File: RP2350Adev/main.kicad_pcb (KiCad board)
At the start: 4 copper layers, 88.9 x 50.9 mm, 111 parts, among them J1 J-Link, J2 SPI Pins, J3 QSPI Pins, J4 UART Pins, J5 UART, J6 DEBUG, J7 USB_A_Male, J8 USB_A_Female, J9 USB4105-GF-A, M1 TS3USB3031RMGR, SW1 SW_DIP_x06, U1 nRF5340-QKxx, U3 LFD_Diplexer, U4 nRF7002-QFAA, U6 W25Q32JV, U7 RP2350A, U8 TS3USB30EDGSR, X1 32.768kHz, X2 32MHz, X3 XTAL-40, X4 IQXO-791

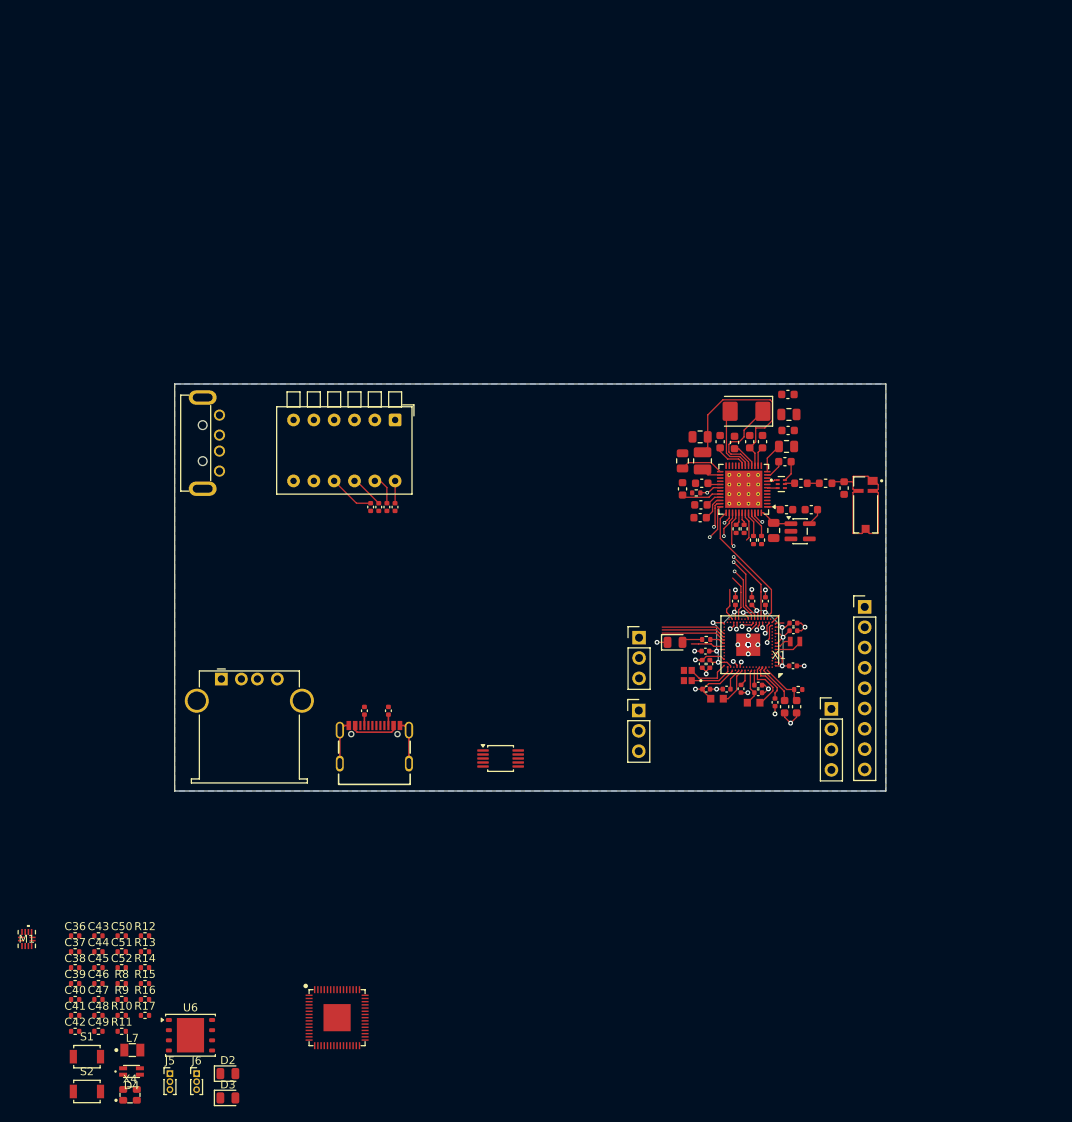
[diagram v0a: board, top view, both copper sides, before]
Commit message: Combine subcircuits
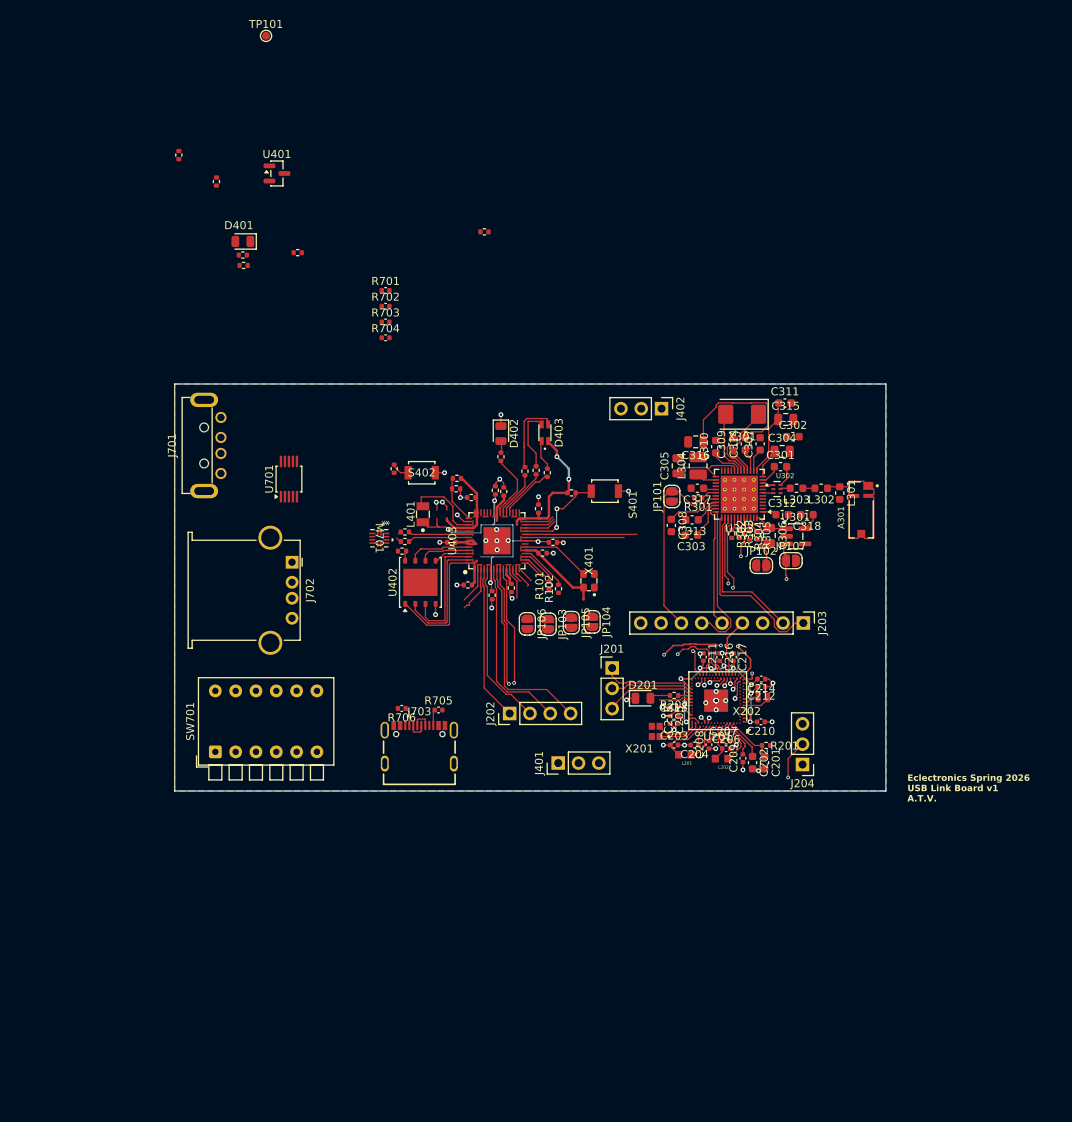
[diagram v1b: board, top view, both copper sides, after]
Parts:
- removed A1: NN03-320, Eclectronics:XCVR_NN03-320
- removed C1, C17, C7, C8, C9: 1.0µF, Capacitor_SMD:C_0402_1005Metric
- removed C10, C9: 100nF, Capacitor_SMD:C_0603_1608Metric
- removed C10, C11, C12, C13, C16, C3, C4, C5, C6: 100nF, Capacitor_SMD:C_0402_1005Metric
- removed C11, C12, C22, C23: 4.7uF, Capacitor_SMD:C_0805_2012Metric
- removed C13: 2.2uF, Capacitor_SMD:C_0805_2012Metric
- removed C14: 22nF, Capacitor_SMD:C_0603_1608Metric
- removed C14, C15: 4.7µF, Capacitor_SMD:C_0603_1608Metric
- removed C15: 0.22uF, Capacitor_SMD:C_0603_1608Metric
- removed C16, C25: 2.2uF, Capacitor_SMD:C_0603_1608Metric
- removed C17, C18, C19, C20: 1uF, Capacitor_SMD:C_0603_1608Metric
- removed C2: 2.2nF, Capacitor_SMD:C_0402_1005Metric
- removed C21, C8: 0.47uF, Capacitor_SMD:C_0603_1608Metric
- removed C24: 10nF, Capacitor_SMD:C_0603_1608Metric
- removed C36, C38: 10µF, Resistor_SMD:R_0402_1005Metric
- removed C37, C41, C42, C43, C44, C45, C46, C47, C50, C52: 0.1µF, Resistor_SMD:R_0402_1005Metric
- removed C39, C40, C48, C49, C51: 4.7µF, Resistor_SMD:R_0402_1005Metric
- removed D1, D3: LED, LED_SMD:LED_0805_2012Metric
- removed D2: PWR, LED_SMD:LED_0805_2012Metric
- removed D4: IN-S85TATRGB, Eclectronics:IN-S85TATRGB
- removed J1: J-Link, Connector_PinHeader_2.54mm:PinHeader_1x03_P2.54mm_Vertical
- removed J2: SPI Pins, Connector_PinHeader_2.54mm:PinHeader_1x04_P2.54mm_Vertical
- removed J3: QSPI Pins, Connector_PinHeader_2.54mm:PinHeader_1x09_P2.54mm_Vertical
- removed J4: UART Pins, Connector_PinHeader_2.54mm:PinHeader_1x03_P2.54mm_Vertical
- removed J5: UART, Connector_PinHeader_1.00mm:PinHeader_1x03_P1.00mm_Vertical
- removed J6: DEBUG, Connector_PinHeader_1.00mm:PinHeader_1x03_P1.00mm_Vertical
- removed J7: USB_A_Male, Eclectronics:USB_A_0480370001
- removed J8: USB_A_Female, Connector_USB:USB_A_Stewart_SS-52100-001_Horizontal
- removed J9: USB4105-GF-A, Eclectronics:USB4105-GF-A
- removed L1: 10uH, Eclectronics:INDC1608X95N
- removed L2: 10µH, Eclectronics:INDC1608X95N
- removed L3: 7.5nH, Inductor_SMD:L_0603_1608Metric
- removed L4, L5: 2.7nH, Inductor_SMD:L_0603_1608Metric
- removed L6: 3.3uH, Inductor_SMD:L_1008_2520Metric
- removed L7: 3.3µH, Eclectronics:AOTA-B201610S3R3-101-T
- removed M1: TS3USB3031RMGR, Eclectronics:RMG12_TEX
- removed R1, R10, R14, R16, R17: 1K, Resistor_SMD:R_0402_1005Metric
- removed R11, R12: 27Ω, Resistor_SMD:R_0402_1005Metric
- removed R13: 33Ω, Resistor_SMD:R_0402_1005Metric
- removed R15, R8, R9: 5.1K, Resistor_SMD:R_0402_1005Metric
- removed R18, R19, R20, R21: 10K, Capacitor_SMD:C_0402_1005Metric
- removed R2: 2.2 Ω, Resistor_SMD:R_0402_1005Metric
- removed R22, R23: 5.1K, Capacitor_SMD:C_0402_1005Metric
- removed R3, R4, R5, R6, R7: 100k, Resistor_SMD:R_0402_1005Metric
- removed S1: RST, Button_Switch_SMD:SW_SPST_B3U-1000P
- removed S2: BOOT, Button_Switch_SMD:SW_SPST_B3U-1000P
- removed SW1: SW_DIP_x06, Button_Switch_THT:SW_DIP_SPSTx06_Piano_10.8x16.8mm_W7.62mm_P2.54mm
- removed U1: nRF5340-QKxx, Package_DFN_QFN:Nordic_AQFN-94-1EP_7x7mm_P0.4mm
- removed U2: ~, Package_TO_SOT_SMD:SC-74A-5_1.55x2.9mm_P0.95mm
- removed U3: LFD_Diplexer, Eclectronics:FIL_LFD182G45DCJD247
- removed U4: nRF7002-QFAA, Package_DFN_QFN:QFN-48-1EP_6x6mm_P0.4mm_EP4.66x4.66mm_ThermalVias
- removed U6: W25Q32JV, Package_SON:WSON-8-1EP_6x5mm_P1.27mm_EP3.4x4.3mm
- removed U7: RP2350A, Eclectronics:RP2350A_QFN-60_EP_7.75x7.75_Pitch0.4mm
- removed U8: TS3USB30EDGSR, Package_SO:VSSOP-10_3x3mm_P0.5mm
- removed X1: 32.768kHz, Eclectronics:XTAL_CM9V-T1A-32.768KHZ-9PF-20PPM-TA-QC
- removed X2: 32MHz, Eclectronics:XTAL_ABM11W-32.0000MHZ-8-D1X-T3
- removed X3: XTAL-40, Crystal:Crystal_SMD_Abracon_ABM3-2Pin_5.0x3.2mm
- removed X4: IQXO-791, Eclectronics:IQXO-791
- added A301: NN03-320, Eclectronics:XCVR_NN03-320, F.Cu at (129.6, 104.0)
- added C201: 4.7µF, Capacitor_SMD:C_0603_1608Metric, F.Cu at (117.5, 135.7)
- added C202: 4.7µF, Capacitor_SMD:C_0603_1608Metric, F.Cu at (116.0, 135.7)
- added C203: 1.0µF, Capacitor_SMD:C_0402_1005Metric, F.Cu at (106.2, 133.4)
- added C204: 100nF, Capacitor_SMD:C_0402_1005Metric, F.Cu at (108.8, 133.4)
- added C205: 2.2nF, Capacitor_SMD:C_0402_1005Metric, F.Cu at (105.8, 130.3)
- added C206: 1.0µF, Capacitor_SMD:C_0402_1005Metric, F.Cu at (112.8, 133.9)
- added C207: 1.0µF, Capacitor_SMD:C_0402_1005Metric, F.Cu at (112.8, 132.9)
- added C208: 1.0µF, Capacitor_SMD:C_0402_1005Metric, F.Cu at (110.6, 133.4)
- added C209: 1.0µF, Capacitor_SMD:C_0402_1005Metric, F.Cu at (114.8, 135.1)
- added C210: 100nF, Capacitor_SMD:C_0402_1005Metric, F.Cu at (117.1, 130.6)
- added C211: 100nF, Capacitor_SMD:C_0402_1005Metric, F.Cu at (109.9, 122.5)
- added C212: 100nF, Capacitor_SMD:C_0402_1005Metric, F.Cu at (117.2, 126.2)
- added C213: 100nF, Capacitor_SMD:C_0402_1005Metric, F.Cu at (106.2, 128.7)
- added C214: 100nF, Capacitor_SMD:C_0402_1005Metric, F.Cu at (117.2, 125.2)
- added C215: 100nF, Capacitor_SMD:C_0402_1005Metric, F.Cu at (106.7, 130.3)
- added C216: 100nF, Capacitor_SMD:C_0402_1005Metric, F.Cu at (112.0, 122.5)
- added C217: 100nF, Capacitor_SMD:C_0402_1005Metric, F.Cu at (113.7, 122.5)
- added C301: 0.47uF, Capacitor_SMD:C_0603_1608Metric, F.Cu at (119.5, 98.7)
- added C302: 100nF, Capacitor_SMD:C_0603_1608Metric, F.Cu at (121.1, 94.9)
- added C303: 100nF, Capacitor_SMD:C_0603_1608Metric, F.Cu at (108.4, 107.2)
- added C304: 4.7uF, Capacitor_SMD:C_0805_2012Metric, F.Cu at (119.8, 96.8)
- added C305: 4.7uF, Capacitor_SMD:C_0805_2012Metric, F.Cu at (106.8, 98.5)
- added C306: 2.2uF, Capacitor_SMD:C_0805_2012Metric, F.Cu at (118.2, 107.2)
- added C307: 22nF, Capacitor_SMD:C_0603_1608Metric, F.Cu at (117.0, 95.8)
- added C308: 0.22uF, Capacitor_SMD:C_0603_1608Metric, F.Cu at (105.9, 106.0)
- added C309: 2.2uF, Capacitor_SMD:C_0603_1608Metric, F.Cu at (113.6, 95.9)
- added C310: 1uF, Capacitor_SMD:C_0603_1608Metric, F.Cu at (111.5, 96.2)
- added C311: 1uF, Capacitor_SMD:C_0603_1608Metric, F.Cu at (120.1, 90.7)
- added C312: 1uF, Capacitor_SMD:C_0603_1608Metric, F.Cu at (119.8, 104.7)
- added C313: 1uF, Capacitor_SMD:C_0603_1608Metric, F.Cu at (108.5, 105.3)
- added C314: 0.47uF, Capacitor_SMD:C_0603_1608Metric, F.Cu at (115.2, 95.8)
- added C315: 4.7uF, Capacitor_SMD:C_0805_2012Metric, F.Cu at (120.2, 92.8)
- added C316: 4.7uF, Capacitor_SMD:C_0805_2012Metric, F.Cu at (109.0, 95.5)
- added C317: 10nF, Capacitor_SMD:C_0603_1608Metric, F.Cu at (109.2, 101.3)
- added C318: 2.2uF, Capacitor_SMD:C_0603_1608Metric, F.Cu at (122.8, 104.7)
- added C401: 10µF, Resistor_SMD:R_0402_1005Metric, F.Cu at (82.5, 69.3)
- added C402: 0.1µF, Resistor_SMD:R_0402_1005Metric, F.Cu at (72.2, 109.2)
- added C403: 10µF, Resistor_SMD:R_0402_1005Metric, F.Cu at (52.4, 73.5)
- added C404: 4.7µF, Resistor_SMD:R_0402_1005Metric, F.Cu at (80.5, 113.4)
- added C405: 4.7µF, Resistor_SMD:R_0402_1005Metric, F.Cu at (83.5, 114.7)
- added C406: 0.1µF, Resistor_SMD:R_0402_1005Metric, F.Cu at (89.8, 109.5)
- added C407: 0.1µF, Resistor_SMD:R_0402_1005Metric, F.Cu at (85.9, 113.8)
- added C408: 0.1µF, Resistor_SMD:R_0402_1005Metric, F.Cu at (85.0, 101.8)
- added C409: 0.1µF, Resistor_SMD:R_0402_1005Metric, F.Cu at (89.3, 103.9)
- added C410: 0.1µF, Resistor_SMD:R_0402_1005Metric, F.Cu at (78.4, 108.1)
- added C411: 0.1µF, Resistor_SMD:R_0402_1005Metric, F.Cu at (80.9, 102.5)
- added C412: 0.1µF, Resistor_SMD:R_0402_1005Metric, F.Cu at (44.3, 59.7)
- added C413: 4.7µF, Resistor_SMD:R_0402_1005Metric, F.Cu at (59.2, 71.9)
- added C414: 4.7µF, Resistor_SMD:R_0402_1005Metric, F.Cu at (79.0, 101.4)
- added C415: 0.1µF, Resistor_SMD:R_0402_1005Metric, F.Cu at (83.9, 101.6)
- added C416: 4.7µF, Resistor_SMD:R_0402_1005Metric, F.Cu at (91.1, 108.1)
- added C417: 0.1µF, Resistor_SMD:R_0402_1005Metric, F.Cu at (49.0, 63.0)
- added D201: LED, LED_SMD:LED_0805_2012Metric, F.Cu at (102.3, 127.6)
- added D401: PWR, LED_SMD:LED_0805_2012Metric, F.Cu at (52.3, 70.5)
- added D402: LED, LED_SMD:LED_0805_2012Metric, F.Cu at (84.6, 94.5)
- added D403: IN-S85TATRGB, Eclectronics:IN-S85TATRGB, F.Cu at (90.1, 94.4)
- added J201: J-Link, Connector_PinHeader_2.54mm:PinHeader_1x03_P2.54mm_Vertical, F.Cu at (98.5, 123.8)
- added J202: SPI Pins, Connector_PinHeader_2.54mm:PinHeader_1x04_P2.54mm_Vertical, F.Cu at (85.7, 129.5)
- added J203: QSPI Pins, Connector_PinHeader_2.54mm:PinHeader_1x09_P2.54mm_Vertical, F.Cu at (122.4, 118.2)
- added J204: UART Pins, Connector_PinHeader_2.54mm:PinHeader_1x03_P2.54mm_Vertical, F.Cu at (122.3, 135.9)
- added J401: UART, Connector_PinHeader_2.54mm:PinHeader_1x03_P2.54mm_Vertical, F.Cu at (91.8, 135.7)
- added J402: DEBUG, Connector_PinHeader_2.54mm:PinHeader_1x03_P2.54mm_Vertical, F.Cu at (104.7, 91.4)
- added J701: USB_A_Male, Eclectronics:USB_A_0480370001, F.Cu at (47.5, 96.0)
- added J702: USB_A_Female, Connector_USB:USB_A_Stewart_SS-52100-001_Horizontal, F.Cu at (58.5, 110.6)
- added J703: USB4105-GF-A, Eclectronics:USB4105-GF-A, F.Cu at (74.4, 135.8)
- added JP101: SolderJumper_2_Open, Jumper:SolderJumper-2_P1.3mm_Open_RoundedPad1.0x1.5mm, F.Cu at (106.0, 102.4)
- added JP102: SolderJumper_2_Open, Jumper:SolderJumper-2_P1.3mm_Open_RoundedPad1.0x1.5mm, F.Cu at (117.2, 111.0)
- added JP103: SolderJumper_2_Open, Jumper:SolderJumper-2_P1.3mm_Open_RoundedPad1.0x1.5mm, F.Cu at (90.5, 118.3)
- added JP104: SolderJumper_2_Open, Jumper:SolderJumper-2_P1.3mm_Open_RoundedPad1.0x1.5mm, F.Cu at (96.0, 118.0)
- added JP105: SolderJumper_2_Open, Jumper:SolderJumper-2_P1.3mm_Open_RoundedPad1.0x1.5mm, F.Cu at (93.4, 118.2)
- added JP106: SolderJumper_2_Open, Jumper:SolderJumper-2_P1.3mm_Open_RoundedPad1.0x1.5mm, F.Cu at (87.9, 118.3)
- added JP107: SolderJumper_2_Open, Jumper:SolderJumper-2_P1.3mm_Open_RoundedPad1.0x1.5mm, F.Cu at (120.8, 110.4)
- added L201: 10uH, Eclectronics:INDC1608X95N, F.Cu at (107.6, 134.7)
- added L202: 10µH, Eclectronics:INDC1608X95N, F.Cu at (112.2, 135.2)
- added L301: 7.5nH, Inductor_SMD:L_0603_1608Metric, F.Cu at (127.0, 102.0)
- added L302: 2.7nH, Inductor_SMD:L_0603_1608Metric, F.Cu at (124.6, 101.3)
- added L303: 2.7nH, Inductor_SMD:L_0603_1608Metric, F.Cu at (121.5, 101.3)
- added L304: 3.3uH, Inductor_SMD:L_1008_2520Metric, F.Cu at (109.2, 98.5)
- added L401: 3.3µH, Eclectronics:AOTA-B201610S3R3-101-T, F.Cu at (74.8, 104.6)
- added M701: TS3USB3031RMGR, Eclectronics:RMG12_TEX, F.Cu at (69.4, 107.6)
- added R101: 27Ω, Resistor_SMD:R_0402_1005Metric, F.Cu at (90.6, 113.5)
- added R102: 27Ω, Resistor_SMD:R_0402_1005Metric, F.Cu at (91.8, 113.9)
- added R201: 2.2 Ω, Resistor_SMD:R_0402_1005Metric, F.Cu at (117.8, 133.5)
- added R202: 1K, Resistor_SMD:R_0402_1005Metric, F.Cu at (106.2, 127.2)
- added R301: 100k, Resistor_SMD:R_0402_1005Metric, F.Cu at (109.2, 102.5)
- added R302: 100k, Resistor_SMD:R_0402_1005Metric, F.Cu at (113.5, 107.0)
- added R303: 100k, Resistor_SMD:R_0402_1005Metric, F.Cu at (114.5, 107.0)
- added R304: 100k, Resistor_SMD:R_0402_1005Metric, F.Cu at (115.7, 107.2)
- added R305: 100k, Resistor_SMD:R_0402_1005Metric, F.Cu at (116.7, 107.2)
- added R401: 5.1K, Resistor_SMD:R_0402_1005Metric, F.Cu at (93.4, 101.9)
- added R402: 5.1K, Resistor_SMD:R_0402_1005Metric, F.Cu at (71.3, 98.9)
- added R403: 1K, Resistor_SMD:R_0402_1005Metric, F.Cu at (52.3, 72.2)
- added R404: 27Ω, Resistor_SMD:R_0402_1005Metric, F.Cu at (72.6, 106.8)
- added R405: 27Ω, Resistor_SMD:R_0402_1005Metric, F.Cu at (72.6, 108.0)
- added R406: 33Ω, Resistor_SMD:R_0402_1005Metric, F.Cu at (79.1, 100.1)
- added R407: 1K, Resistor_SMD:R_0402_1005Metric, F.Cu at (90.4, 99.4)
- added R408: 5.1K, Resistor_SMD:R_0402_1005Metric, F.Cu at (89.0, 99.1)
- added R409: 1K, Resistor_SMD:R_0402_1005Metric, F.Cu at (87.6, 99.2)
- added R410: 1K, Resistor_SMD:R_0402_1005Metric, F.Cu at (84.6, 97.4)
- added R701: 10K, Capacitor_SMD:C_0402_1005Metric, F.Cu at (70.2, 76.6)
- added R702: 10K, Capacitor_SMD:C_0402_1005Metric, F.Cu at (70.2, 78.6)
- added R703: 10K, Capacitor_SMD:C_0402_1005Metric, F.Cu at (70.2, 80.6)
- added R704: 10K, Capacitor_SMD:C_0402_1005Metric, F.Cu at (70.2, 82.5)
- added R705: 5.1K, Capacitor_SMD:C_0402_1005Metric, F.Cu at (76.8, 129.1)
- added R706: 5.1K, Capacitor_SMD:C_0402_1005Metric, F.Cu at (72.2, 128.9)
- added S401: RST, Button_Switch_SMD:SW_SPST_B3U-1000P, F.Cu at (97.6, 101.7)
- added S402: BOOT, Button_Switch_SMD:SW_SPST_B3U-1000P, F.Cu at (74.7, 99.4)
- added SW701: SW_DIP_x06, Button_Switch_THT:SW_DIP_SPSTx06_Piano_10.8x16.8mm_W7.62mm_P2.54mm, F.Cu at (48.9, 134.3)
- added TP101: TestPoint, TestPoint:TestPoint_Pad_D1.0mm, F.Cu at (55.2, 44.8)
- added U201: nRF5340-QKxx, Package_DFN_QFN:Nordic_AQFN-94-1EP_7x7mm_P0.4mm, F.Cu at (111.7, 127.9)
- added U301: ~, Package_TO_SOT_SMD:SC-74A-5_1.55x2.9mm_P0.95mm, F.Cu at (121.5, 107.3)
- added U302: LFD_Diplexer, Eclectronics:FIL_LFD182G45DCJD247, F.Cu at (119.1, 101.5)
- added U303: nRF7002-QFAA, Package_DFN_QFN:QFN-48-1EP_6x6mm_P0.4mm_EP4.66x4.66mm_ThermalVias, F.Cu at (114.4, 102.1)
- added U401: MCP1702T-3302E_CB, Package_TO_SOT_SMD:SOT-23, F.Cu at (56.6, 62.0)
- added U402: W25Q32JV, Package_SON:WSON-8-1EP_6x5mm_P1.27mm_EP3.4x4.3mm, F.Cu at (74.5, 113.1)
- added U403: RP2350A, Eclectronics:RP2350A_QFN-60_EP_7.75x7.75_Pitch0.4mm, F.Cu at (84.1, 107.9)
- added U701: TS3USB30EDGSR, Package_SO:VSSOP-10_3x3mm_P0.5mm, F.Cu at (58.1, 100.2)
- added X201: 32MHz, Eclectronics:XTAL_ABM11W-32.0000MHZ-8-D1X-T3, F.Cu at (104.0, 131.8)
- added X202: 32.768kHz, Eclectronics:XTAL_CM9V-T1A-32.768KHZ-9PF-20PPM-TA-QC, F.Cu at (117.3, 127.5)
- added X301: XTAL-40, Crystal:Crystal_SMD_Abracon_ABM3-2Pin_5.0x3.2mm, F.Cu at (114.8, 92.1)
- added X401: IQXO-791, Eclectronics:IQXO-791, F.Cu at (95.6, 112.9)
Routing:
- net +3V3: track 59.7 -> 129.9 mm, vias 10 -> 12
- net /RP2350Adev/SPI_MOSI: track 0.00 -> 55.6 mm, vias 0 -> 1
- net /RP2350Adev/SPI_MISO: track 0.00 -> 54.9 mm, vias 0 -> 3
- net /RP2350Adev/SPI_SS: track 0.00 -> 48.7 mm, vias 0 -> 1
- net +1V1: track 0.00 -> 42.7 mm, vias 0 -> 4
- net /RP2350Adev/MUX2_OE: track 4.19 -> 44.8 mm, vias 0 -> 2
- net /RP2350Adev/MUX2_S: track 5.71 -> 45.0 mm, vias 0 -> 2
- net Net-(A1-A): track 24.5 -> 0.00 mm
- net Net-(A301-A): track 0.00 -> 24.5 mm
- net /nRF5340/IOVDD_EN: track 4.16 -> 26.6 mm, vias 0 -> 2
- net /RP2350Adev/SPI_CLK: track 0.00 -> 22.0 mm, vias 0 -> 1
- net /nRF5340/RX: track 0.92 -> 21.8 mm, vias 1 -> 2
- net /RP2350Adev/BOOT: track 0.00 -> 19.4 mm
- net /nRF5340/TX: track 0.69 -> 17.0 mm
- net Net-(U402-DO/IO1): track 0.00 -> 15.9 mm
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- added copper zone on F.Cu, net +3V3
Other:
- board text added: "Eclectronics Spring 2026 USB Link Board v1 A.T.V."

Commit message: Layout mostly complete, need to finalize layers
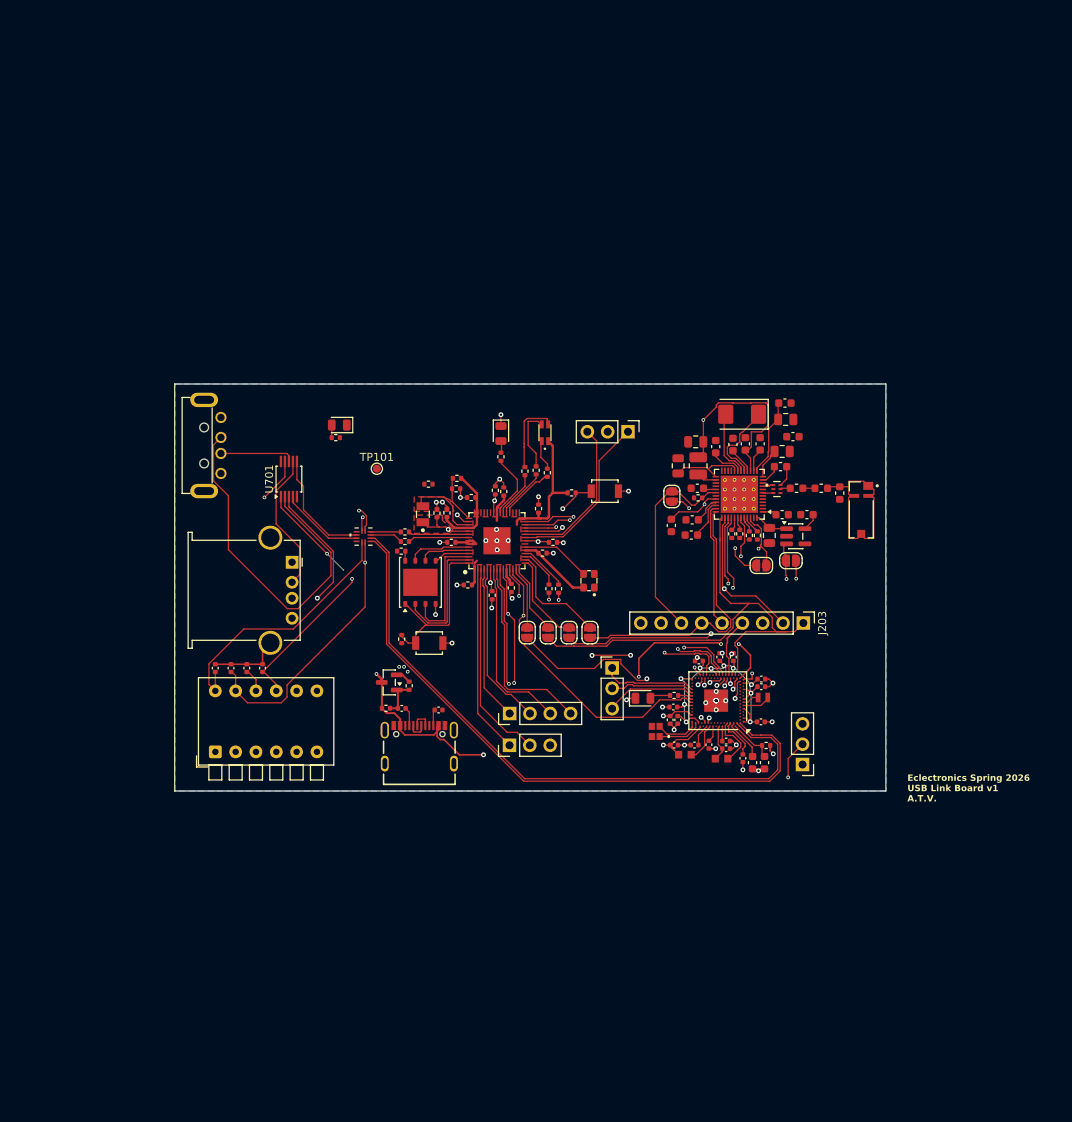
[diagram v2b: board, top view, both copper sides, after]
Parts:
- moved U401 65.1 mm to (70.6, 125.6), turned to 180 degrees
- moved C401 60.8 mm to (70.2, 128.9), turned to 180 degrees
- moved C403 56.5 mm to (73.1, 126.0), turned to -90 degrees
- moved C412 55.9 mm to (77.9, 104.4), turned to -90 degrees
- moved TP101 55.9 mm to (69.1, 98.9)
- moved R701 51.8 mm to (48.9, 123.8), turned to 90 degrees
- moved C417 49.8 mm to (76.6, 104.5), turned to -90 degrees
- moved R702 49.2 mm to (50.9, 123.8), turned to 90 degrees
- moved R703 46.6 mm to (52.8, 123.8), turned to 90 degrees
- moved R704 44.1 mm to (54.8, 123.8), turned to 90 degrees
- moved C413 33.2 mm to (75.5, 100.8)
- moved D401 25.9 mm to (64.4, 93.4)
- moved R403 25.6 mm to (64.0, 95.0)
- moved R402 21.3 mm to (72.2, 120.2)
- moved S402 21.3 mm to (75.6, 120.7)
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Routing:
- net +5V: track 0.00 -> 111.4 mm, vias 0 -> 3
- net /RP2350Adev/MUX1_S0: track 6.38 -> 114.6 mm, vias 0 -> 1
- net /RP2350Adev/MUX2_S: track 45.0 -> 134.0 mm, vias 2 -> 4
- net /RP2350Adev/MUX1_S1: track 5.11 -> 86.3 mm, vias 1 -> 5
- net /USB_Mux_Periph/D1+: track 0.00 -> 80.3 mm
- net /USB_Mux_Periph/D1-: track 0.00 -> 79.9 mm
- net /RP2350Adev/MUX2_OE: track 44.8 -> 114.2 mm, vias 2 -> 4
- net Net-(J701-D+): track 0.00 -> 45.0 mm
- net /nRF5340/QSPI0: track 26.1 -> 63.9 mm
- net /RP2350Adev/IOVDD_EN: track 3.75 -> 39.6 mm, vias 0 -> 2
- net /USB_Mux_Periph/D3+: track 0.00 -> 35.2 mm, vias 0 -> 2
- net /USB_Mux_Periph/D3-: track 0.00 -> 33.7 mm, vias 0 -> 2
- net /RP2350Adev/SPI_CLK: track 22.0 -> 53.2 mm
- net /nRF5340/QSPI_CLK: track 25.4 -> 53.1 mm, vias 1 -> 2
- net /RP2350Adev/HOST_IRQ: track 4.10 -> 31.7 mm, vias 0 -> 2
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- added copper zone on F.Cu, net +1V1
- added copper zone on In2.Cu, net +3V3
- added copper zone on F.Cu, net GND
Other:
- board text added: "C405"

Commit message: RF layout
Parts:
- U201: footprint Package_DFN_QFN:Nordic_AQFN-94-1EP_7x7mm_P0.4mm -> Eclectronics:Nordic_AQFN-94-1EP_7x7mm_P0.4mm
- U303: footprint Package_DFN_QFN:QFN-48-1EP_6x6mm_P0.4mm_EP4.66x4.66mm_ThermalVias -> Package_DFN_QFN:QFN-48-1EP_6x6mm_P0.4mm_EP4.6x4.6mm
- moved TP101 26.5 mm to (92.3, 111.6)
- moved C318 21.1 mm to (103.4, 96.5)
- moved J701 18.7 mm to (46.7, 114.7)
- moved C315 17.7 mm to (103.3, 98.3), turned to 180 degrees
- moved J702 16.0 mm to (57.3, 94.7)
- moved C311 15.6 mm to (105.9, 97.2), turned to -90 degrees
- moved L301 14.6 mm to (123.9, 116.2)
- moved L302 12.0 mm to (123.0, 113.2), turned to 90 degrees
- moved U701 11.6 mm to (59.1, 111.8)
- moved C305 10.2 mm to (116.7, 96.2), turned to 180 degrees
- moved C316 9.05 mm to (102.4, 101.8), turned to -90 degrees
- moved L303 8.87 mm to (123.0, 110.1), turned to 90 degrees
- moved A301 8.45 mm to (129.8, 112.5), turned to -90 degrees
- moved X401 6.18 mm to (89.8, 110.8)
- moved R403 5.82 mm to (69.7, 96.2)
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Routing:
- net GND: track 53.7 -> 132.4 mm, vias 56 -> 131
- net +3V3: track 129.6 -> 171.9 mm, vias 10 -> 31
- net Net-(J701-D+): track 45.0 -> 11.5 mm
- net Net-(A301-A): track 24.5 -> 7.28 mm
- net /RP2350Adev/MUX2_S: track 134.0 -> 117.6 mm, vias 4 -> 3
- net +5V: track 111.4 -> 126.1 mm
- net /RP2350Adev/MUX2_OE: track 114.2 -> 101.1 mm
- net /RP2350Adev/MUX1_S0: track 114.6 -> 101.5 mm, vias 1 -> 2
- net Net-(U303-PALDO): track 3.75 -> 15.9 mm, vias 0 -> 2
- net /nRF7002/PWR_IOVDD: track 6.68 -> 17.9 mm, vias 0 -> 2
- net Net-(M701-D-): track 14.3 -> 4.58 mm
- net Net-(U302-COM): track 1.25 -> 10.2 mm
- net /nRF5340/QSPI1: track 54.3 -> 61.5 mm, vias 3 -> 2
- net Net-(J701-D-): track 9.34 -> 16.4 mm
- net /nRF7002/VDD_BUCK: track 42.0 -> 35.0 mm, vias 2 -> 3
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
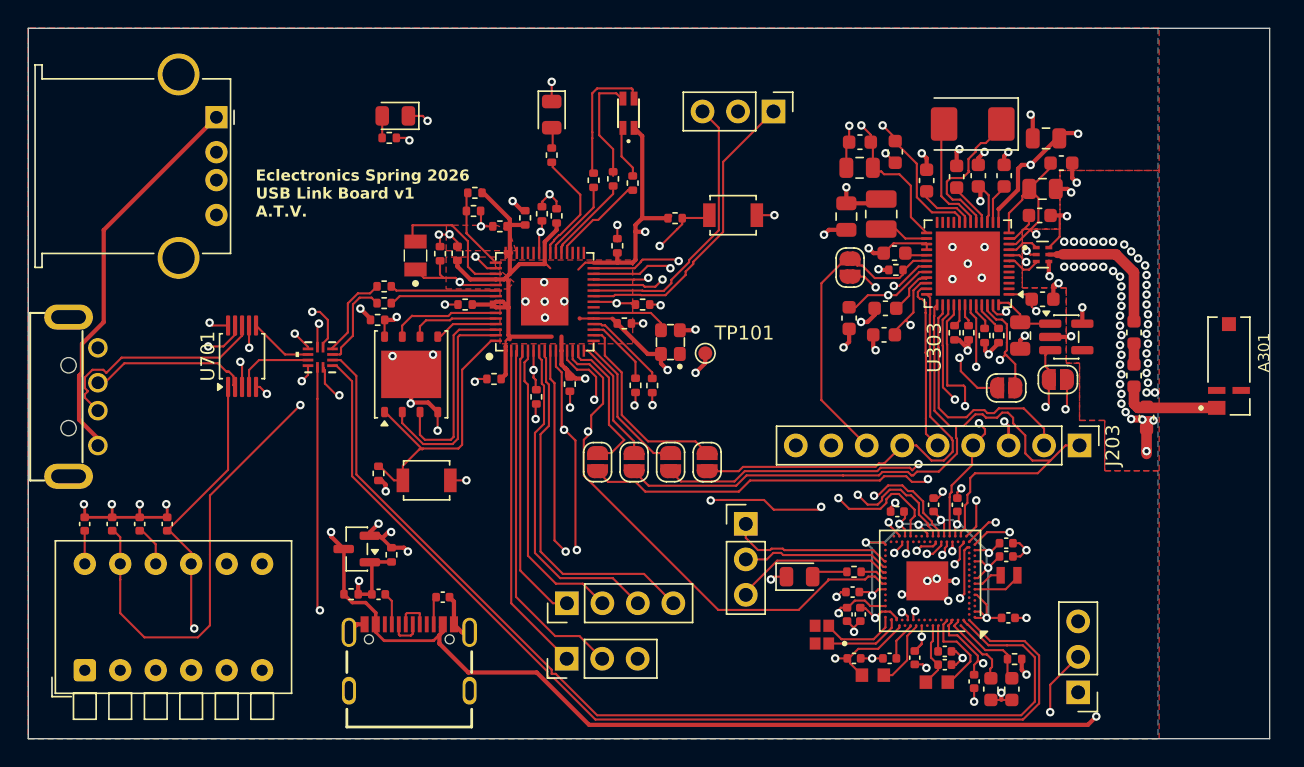
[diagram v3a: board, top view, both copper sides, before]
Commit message: Pushing Added Arts, Fixes to Overlapping Labels
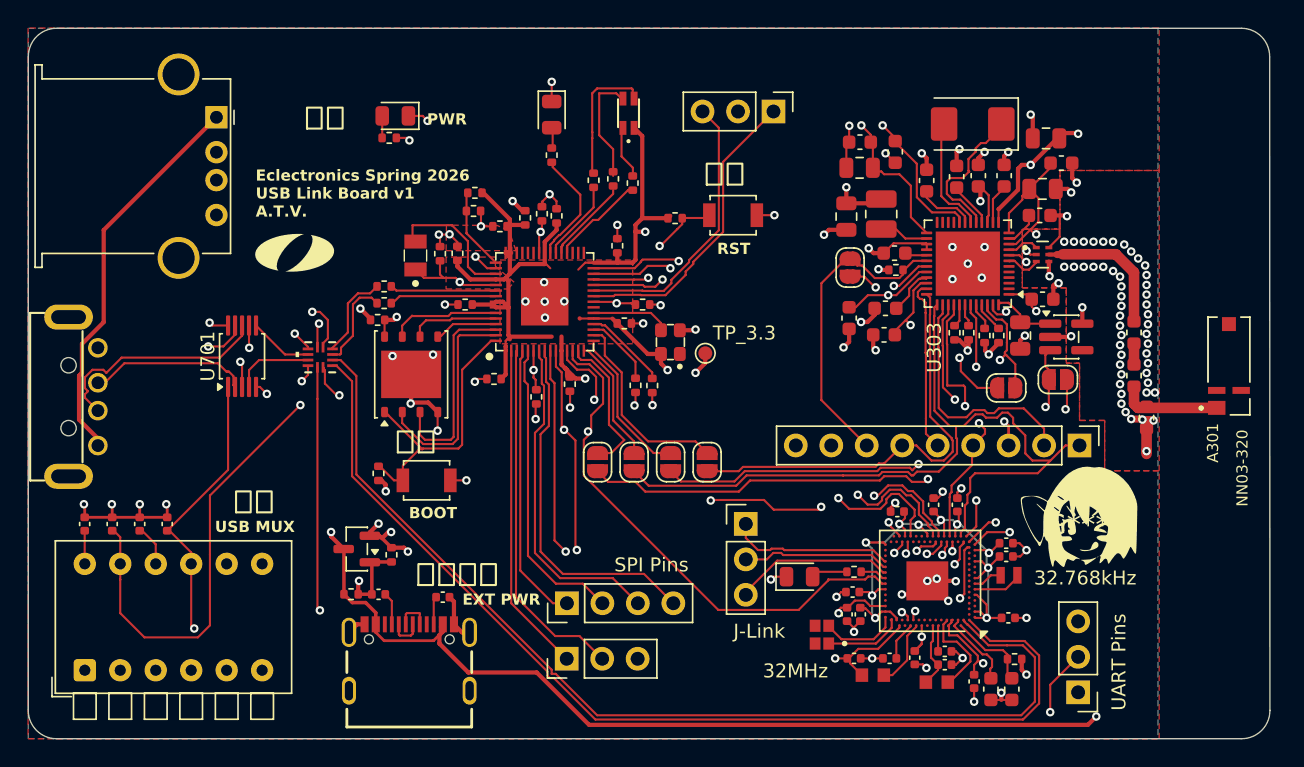
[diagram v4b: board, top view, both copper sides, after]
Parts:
- added G***: LOGO, LOGO, F.Cu at (118.9, 123.9)
- added G***: LOGO, LOGO, B.Cu at (70.3, 112.8)
- added OlinLogo: G***, Eclectronics:OlinLogo, F.Cu at (62.9, 104.4)
- renumbered TP101 to TP_3.3
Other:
- outline, holes or cut-outs redrawn
- board text added: "Allan Huang Trinity Lee Venkadesh Eswaranadam"
- board text added: "BOOT"
- board text added: "DHMICRO"
- board text added: "EXT PWR"
- board text added: "PWR"
- board text added: "RST"
- board text added: "USB MUX"
- board text added: "切替"
- board text added: "啟動"
- board text added: "外部電源"
- board text added: "重置"
- board text added: "金龍電子 HB7002 2616 TAIWAN/NEEDHAM"
- board text added: "電源"
